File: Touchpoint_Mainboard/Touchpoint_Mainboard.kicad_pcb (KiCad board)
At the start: 2 copper layers, 92.8 x 86.6 mm, 95 parts, among them J1 USB4105-GF-A, J2 Conn_01x02, J3 Conn_01x10, J4 Conn_01x32, J5 Conn_01x32, SW1 SW_SPST, SW2 SW_SPST, SW3 SW_SPST, U1 Val**, U2 USBLC6-2SC6, U3 TLS105B0MBHTSA1, U4 NCP1117-3.3_SOT223, U5 W25Q128JVS, U6 RP2040, U7 DRV2605LDGS, U8 BNO055, U9 HV507PG-G, Y1 ABM8-272-T3, Y2 Crystal

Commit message: Added board outlines
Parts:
- moved S1 70.2 mm to (26.5, 65.2)
- moved U9 22.3 mm to (51.4, 20.2)
- moved J4 17.8 mm to (33.5, 51.6)
- moved J5 9.24 mm to (44.6, 57.2)
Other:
- board size 92.8 x 86.6 mm -> 58 x 96.4 mm
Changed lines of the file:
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@@
 	(footprint "Touchpoint:HRS_FH34SRJ-32S-0.5SH_50_"
 		(layer "F.Cu")
-		(at 49.63 59.205)
+		(at 33.55 51.65)
 		(property "Reference" "J4"
 			(at -6.968 -2.7564 0)
@@
 	(footprint "Touchpoint:HRS_FH34SRJ-32S-0.5SH_50_"
 		(layer "F.Cu")
-		(at 49.63 65.03)
+		(at 44.65 57.25)
 		(property "Reference" "J5"
 			(at -6.968 -2.7564 0)
@@
 	(footprint "Package_QFP:PQFP-80_14x20mm_P0.8mm"
 		(layer "F.Cu")
-		(at 50.2991 42.5163)
+		(at 51.4 20.2)
 		(descr "PQFP, 80 Pin (JEITA/EIAJ ED-7311A (variation 80-001-PB) / JEDEC MS-022 (variation GB-2), 2.70mm body thickness, https://www.jeita.or.jp/japanese/standard/book/ED-7311A/#target/page_no=91, https://www.jedec.org/document_search?search_api_views_fulltext=MS-022), generated with kicad-footprint-generator ipc_gullwing_generator.py")
 		(tags "PQFP QFP P-QFP080-14.00x20.00-0.80 P-QFP080-1420-0.80 MQFP-80 Onsemi_PQFP80-14x20-/-QIP80E Onsemi_CASE-122BS")
@@
 	(footprint "Touchpoint:XDCR_PEC12R-4220F-S0024"
 		(layer "F.Cu")
-		(at 93.21 87.105)
+		(at 26.5 65.2)
 		(property "Reference" "S1"
 			(at -3.075 -9.385 0)
@@
 		)
 	)
-	(gr_rect
-		(start 28 22.6)
-		(end 120.8 109.2)
+	(gr_arc
+		(start 75.5 113.4)
+		(mid 74.62132 115.52132)
+		(end 72.5 116.4)
 		(stroke
-			(width 0.05)
+			(width 0.1)
+			(type default)
+		)
+		(layer "Edge.Cuts")
+	)
+	(gr_arc
+		(start 73.293799 23.706925)
+		(mid 74.885518 24.780851)
+		(end 75.499999 26.6)
+		(stroke
+			(width 0.1)
+			(type default)
+		)
+		(layer "Edge.Cuts")
+	)
+	(gr_arc
+		(start 45.774 20)
+		(mid 59.658169 20.930897)
+		(end 73.293799 23.706925)
+		(stroke
+			(width 0.1)
+			(type default)
+		)
+		(layer "Edge.Cuts")
+	)
+	(gr_arc
+		(start 17.5 59)
+		(mid 18.37868 56.87868)
+		(end 20.5 56)
+		(stroke
+			(width 0.1)
+			(type default)
+		)
+		(layer "Edge.Cuts")
+	)
+	(gr_line
+		(start 75.5 113.4)
+		(end 75.5 26.6)
+		(stroke
+			(width 0.1)
+			(type default)
+		)
+		(layer "Edge.Cuts")
+	)
+	(gr_arc
+		(start 20.5 74)
+		(mid 18.37868 73.12132)
+		(end 17.5 71)
+		(stroke
+			(width 0.1)
+			(type default)
+		)
+		(layer "Edge.Cuts")
+	)
+	(gr_circle
+		(center 27.5 113.4)
+		(end 28.75 113.4)
+		(stroke
+			(width 0.1)
 			(type default)
 		)
@@
 		(layer "Edge.Cuts")
 	)
+	(gr_circle
+		(center 72.5 113.4)
+		(end 73.75 113.4)
+		(stroke
+			(width 0.1)
+			(type default)
+		)
+		(fill no)
+		(layer "Edge.Cuts")
+	)
+	(gr_line
+		(start 24.5 77)
+		(end 24.5 113.4)
+		(stroke
+			(width 0.1)
+			(type default)
+		)
+		(layer "Edge.Cuts")
+	)
+	(gr_arc
+		(start 22.5 54)
+		(mid 21.914214 55.414214)
+		(end 20.5 56)
+		(stroke
+			(width 0.1)
+			(type default)
+		)
+		(layer "Edge.Cuts")
+	)
+	(gr_circle
+		(center 72.5 26.6)
+		(end 73.75 26.6)
+		(stroke
+			(width 0.1)
+			(type default)
+		)
+		(fill no)
+		(layer "Edge.Cuts")
+	)
+	(gr_line
+		(start 27.5 116.4)
+		(end 72.5 116.4)
+		(stroke
+			(width 0.1)
+			(type default)
+		)
+		(layer "Edge.Cuts")
+	)
+	(gr_line
+		(start 45.774 20)
+		(end 45.774 48.393398)
+		(stroke
+			(width 0.1)
+			(type default)
+		)
+		(layer "Edge.Cuts")
+	)
+	(gr_arc
+		(start 21.5 74)
+		(mid 23.62132 74.87868)
+		(end 24.5 77)
+		(stroke
+			(width 0.1)
+			(type default)
+		)
+		(layer "Edge.Cuts")
+	)
+	(gr_line
+		(start 20.5 74)
+		(end 21.5 74)
+		(stroke
+			(width 0.1)
+			(type default)
+		)
+		(layer "Edge.Cuts")
+	)
+	(gr_line
+		(start 17.5 59)
+		(end 17.5 71)
+		(stroke
+			(width 0.1)
+			(type default)
+		)
+		(layer "Edge.Cuts")
+	)
+	(gr_line
+		(start 45.774 48.393398)
+		(end 22.5 48.393398)
+		(stroke
+			(width 0.1)
+			(type default)
+		)
+		(layer "Edge.Cuts")
+	)
+	(gr_arc
+		(start 27.5 116.4)
+		(mid 25.37868 115.52132)
+		(end 24.5 113.4)
+		(stroke
+			(width 0.1)
+			(type default)
+		)
+		(layer "Edge.Cuts")
+	)
+	(gr_line
+		(start 75.499999 26.6)
+		(end 75.5 26.6)
+		(stroke
+			(width 0.1)
+			(type default)
+		)
+		(layer "Edge.Cuts")
+	)
+	(gr_line
+		(start 22.5 48.393398)
+		(end 22.5 54)
+		(stroke
+			(width 0.1)
+			(type default)
+		)
+		(layer "Edge.Cuts")
+	)
+	(group ""
+		(members "1ad37e4e-b6b9-4e6c-85cd-ed556f3a292c" "1f15dedb-0437-4dfb-ae23-e06151dff8a7"
+			"384e42fa-73e4-41a3-84f7-e9f9c41559e0" "47475eac-2ab4-45c5-95f0-45e9eafb9d45"
+			"564b8633-460f-4799-a05d-fa6b9ba46c10" "59d84e67-391c-475e-a263-9467b0be49d6"
+			"5eb19d0c-8374-4a37-a640-12a2215da28b" "749fe87c-5c5e-421b-8f5d-6bd183711101"
+			"7869b034-dd6f-4ae0-8c83-cb25c2b790da" "7aa5406c-3b5b-48c6-bd30-5929644f4599"
+			"7af53521-808f-4e3f-b5eb-59ee0ddbbfe0" "7d954ace-691f-42e0-a6fb-9b1f51016df9"
+			"8805d26e-9c2e-4421-aad2-d2b63194ac1a" "8a445dff-6ab7-4ad5-b9b4-08da110718ff"
+			"9420a9da-29d4-42b2-920b-35abd85438c4" "bc84ea02-31a3-47b7-b687-2b36f0824224"
+			"c3546a9e-decd-4ad4-8e89-77d62777b754" "dafaadef-9b83-4f39-a3b5-75b4cc390f7e"
+			"fd64aab9-eb43-48ae-b4d6-ee88409c8e24" "fda1417a-2a9a-4c05-b2f4-14c45e58f9d0"
+		)
+	)
 	(embedded_fonts no)

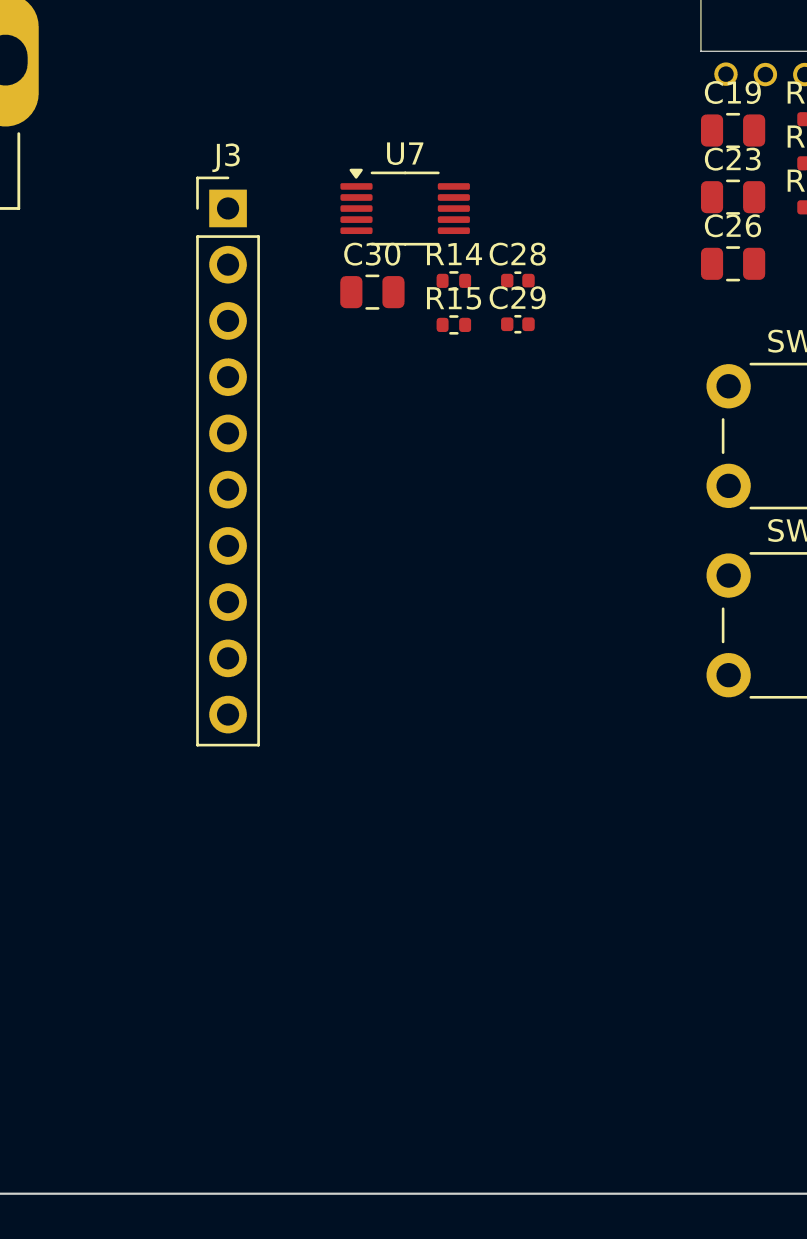
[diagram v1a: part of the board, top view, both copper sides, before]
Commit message: Changed to jumper connector between boards
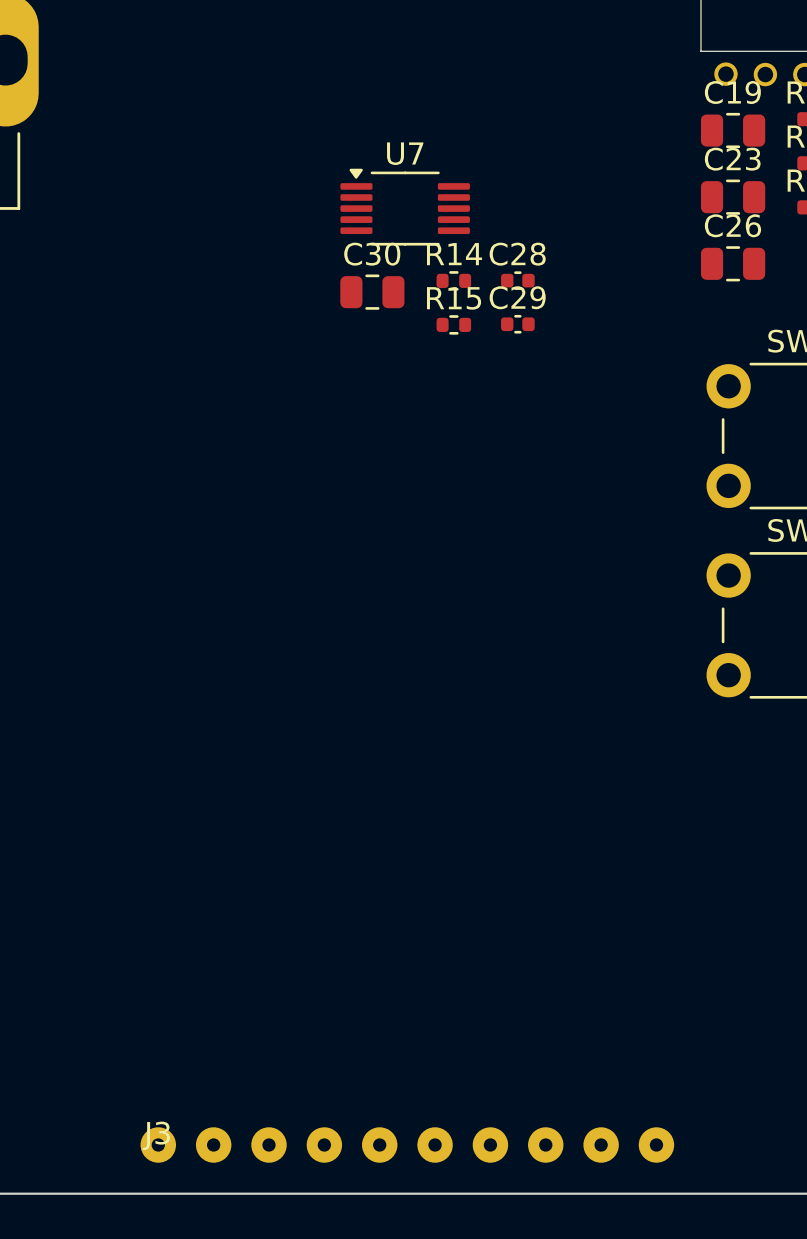
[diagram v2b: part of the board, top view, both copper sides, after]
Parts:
- J3: footprint Connector_PinHeader_2.54mm:PinHeader_1x10_P2.54mm_Vertical -> Touchpoint:Jumper_Interface_10
- U1: value Val** -> PMW3360DM
- moved J3 42.4 mm to (39.0, 114.2)
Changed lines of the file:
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@@
 	(net 163 "/EEOP_Driver/DOUT")
 	(net 164 "unconnected-(U9-NC-Pad36)")
-	(footprint "Connector_PinHeader_2.54mm:PinHeader_1x10_P2.54mm_Vertical"
+	(footprint "Touchpoint:Jumper_Interface_10"
 		(layer "F.Cu")
-		(at 42.15 71.9)
-		(descr "Through hole straight pin header, 1x10, 2.54mm pitch, single row")
-		(tags "Through hole pin header THT 1x10 2.54mm single row")
+		(at 39 114.2)
 		(property "Reference" "J3"
-			(at 0 -2.38 0)
+			(at 0 -0.5 0)
+			(unlocked yes)
 			(layer "F.SilkS")
 			(effects
 				(font
 					(size 1 1)
-					(thickness 0.15)
+					(thickness 0.1)
 				)
 			)
 		)
 		(property "Value" "Conn_01x10"
-			(at 0 25.24 0)
+			(at 0 1 0)
+			(unlocked yes)
 			(layer "F.Fab")
 			(effects
@@
 		(property "Datasheet" "~"
 			(at 0 0 0)
+			(unlocked yes)
 			(layer "F.Fab")
 			(hide yes)
 			(effects
 				(font
-					(size 1.27 1.27)
+					(size 1 1)
 					(thickness 0.15)
 				)
@@
 		(property "Description" "Generic connector, single row, 01x10, script generated (kicad-library-utils/schlib/autogen/connector/)"
 			(at 0 0 0)
+			(unlocked yes)
 			(layer "F.Fab")
 			(hide yes)
 			(effects
 				(font
-					(size 1.27 1.27)
+					(size 1 1)
 					(thickness 0.15)
 				)
@@
 		(sheetname "/Topboard_interface/")
 		(sheetfile "Topboard_interface.kicad_sch")
-		(attr through_hole)
-		(fp_line
-			(start -1.38 -1.38)
-			(end 0 -1.38)
-			(stroke
-				(width 0.12)
-				(type solid)
-			)
-			(layer "F.SilkS")
-		)
-		(fp_line
-			(start -1.38 0)
-			(end -1.38 -1.38)
-			(stroke
-				(width 0.12)
-				(type solid)
-			)
-			(layer "F.SilkS")
-		)
-		(fp_line
-			(start -1.38 1.27)
-			(end -1.38 24.24)
-			(stroke
-				(width 0.12)
-				(type solid)
-			)
-			(layer "F.SilkS")
-		)
-		(fp_line
-			(start -1.38 1.27)
-			(end 1.38 1.27)
-			(stroke
-				(width 0.12)
-				(type solid)
-			)
-			(layer "F.SilkS")
-		)
-		(fp_line
-			(start -1.38 24.24)
-			(end 1.38 24.24)
-			(stroke
-				(width 0.12)
-				(type solid)
-			)
-			(layer "F.SilkS")
-		)
-		(fp_line
-			(start 1.38 1.27)
-			(end 1.38 24.24)
-			(stroke
-				(width 0.12)
-				(type solid)
-			)
-			(layer "F.SilkS")
-		)
-		(fp_line
-			(start -1.77 -1.77)
-			(end -1.77 24.63)
-			(stroke
-				(width 0.05)
-				(type solid)
-			)
-			(layer "F.CrtYd")
-		)
-		(fp_line
-			(start -1.77 24.63)
-			(end 1.77 24.63)
-			(stroke
-				(width 0.05)
-				(type solid)
-			)
-			(layer "F.CrtYd")
-		)
-		(fp_line
-			(start 1.77 -1.77)
-			(end -1.77 -1.77)
-			(stroke
-				(width 0.05)
-				(type solid)
-			)
-			(layer "F.CrtYd")
-		)
-		(fp_line
-			(start 1.77 24.63)
-			(end 1.77 -1.77)
-			(stroke
-				(width 0.05)
-				(type solid)
-			)
-			(layer "F.CrtYd")
-		)
-		(fp_line
-			(start -1.27 -0.635)
-			(end -0.635 -1.27)
-			(stroke
-				(width 0.1)
-				(type solid)
-			)
-			(layer "F.Fab")
-		)
-		(fp_line
-			(start -1.27 24.13)
-			(end -1.27 -0.635)
-			(stroke
-				(width 0.1)
-				(type solid)
-			)
-			(layer "F.Fab")
-		)
-		(fp_line
-			(start -0.635 -1.27)
-			(end 1.27 -1.27)
-			(stroke
-				(width 0.1)
-				(type solid)
-			)
-			(layer "F.Fab")
-		)
-		(fp_line
-			(start 1.27 -1.27)
-			(end 1.27 24.13)
-			(stroke
-				(width 0.1)
-				(type solid)
-			)
-			(layer "F.Fab")
-		)
-		(fp_line
-			(start 1.27 24.13)
-			(end -1.27 24.13)
-			(stroke
-				(width 0.1)
-				(type solid)
-			)
-			(layer "F.Fab")
-		)
+		(attr smd)
 		(fp_text user "${REFERENCE}"
-			(at 0 11.43 90)
+			(at 0 2.5 0)
+			(unlocked yes)
 			(layer "F.Fab")
 			(effects
@@
 			)
 		)
-		(pad "1" thru_hole rect
+		(pad "1" thru_hole circle
 			(at 0 0)
-			(size 1.7 1.7)
-			(drill 1)
+			(size 1.6 1.6)
+			(drill 0.6)
 			(layers "*.Cu" "*.Mask")
 			(remove_unused_layers no)
@@
 		)
 		(pad "2" thru_hole circle
-			(at 0 2.54)
-			(size 1.7 1.7)
-			(drill 1)
+			(at 2.5 0)
+			(size 1.6 1.6)
+			(drill 0.6)
 			(layers "*.Cu" "*.Mask")
 			(remove_unused_layers no)
@@
 		)
 		(pad "3" thru_hole circle
-			(at 0 5.08)
-			(size 1.7 1.7)
-			(drill 1)
+			(at 5 0)
+			(size 1.6 1.6)
+			(drill 0.6)
 			(layers "*.Cu" "*.Mask")
 			(remove_unused_layers no)
@@
 		)
 		(pad "4" thru_hole circle
-			(at 0 7.62)
-			(size 1.7 1.7)
-			(drill 1)
+			(at 7.5 0)
+			(size 1.6 1.6)
+			(drill 0.6)
 			(layers "*.Cu" "*.Mask")
 			(remove_unused_layers no)
@@
 		)
 		(pad "5" thru_hole circle
-			(at 0 10.16)
-			(size 1.7 1.7)
-			(drill 1)
+			(at 10 0)
+			(size 1.6 1.6)
+			(drill 0.6)
 			(layers "*.Cu" "*.Mask")
 			(remove_unused_layers no)
@@
 		)
 		(pad "6" thru_hole circle
-			(at 0 12.7)
-			(size 1.7 1.7)
-			(drill 1)
+			(at 12.5 0)
+			(size 1.6 1.6)
+			(drill 0.6)
 			(layers "*.Cu" "*.Mask")
 			(remove_unused_layers no)
@@
 		)
 		(pad "7" thru_hole circle
-			(at 0 15.24)
-			(size 1.7 1.7)
-			(drill 1)
+			(at 15 0)
+			(size 1.6 1.6)
+			(drill 0.6)
 			(layers "*.Cu" "*.Mask")
 			(remove_unused_layers no)
@@
 		)
 		(pad "8" thru_hole circle
-			(at 0 17.78)
-			(size 1.7 1.7)
-			(drill 1)
+			(at 17.5 0)
+			(size 1.6 1.6)
+			(drill 0.6)
 			(layers "*.Cu" "*.Mask")
 			(remove_unused_layers no)
@@
 		)
 		(pad "9" thru_hole circle
-			(at 0 20.32)
-			(size 1.7 1.7)
-			(drill 1)
+			(at 20 0)
+			(size 1.6 1.6)
+			(drill 0.6)
 			(layers "*.Cu" "*.Mask")
 			(remove_unused_layers no)
@@
 		)
 		(pad "10" thru_hole circle
-			(at 0 22.86)
-			(size 1.7 1.7)
-			(drill 1)
+			(at 22.5 0)
+			(size 1.6 1.6)
+			(drill 0.6)
 			(layers "*.Cu" "*.Mask")
 			(remove_unused_layers no)
@@
 		)
 		(embedded_fonts no)
-		(model "${KICAD9_3DMODEL_DIR}/Connector_PinHeader_2.54mm.3dshapes/PinHeader_1x10_P2.54mm_Vertical.step"
-			(offset
-				(xyz 0 0 0)
-			)
-			(scale
-				(xyz 1 1 1)
-			)
-			(rotate
-				(xyz 0 0 0)
-			)
-		)
 	)
 	(footprint "Resistor_SMD:R_0402_1005Metric"
@@
 			)
 		)
-		(property "Value" "Val**"
+		(property "Value" "PMW3360DM"
 			(at 0 0 0)
 			(layer "F.Fab")
